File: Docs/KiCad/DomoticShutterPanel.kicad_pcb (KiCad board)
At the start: 2 copper layers, 110.6 x 50 mm, 7 parts

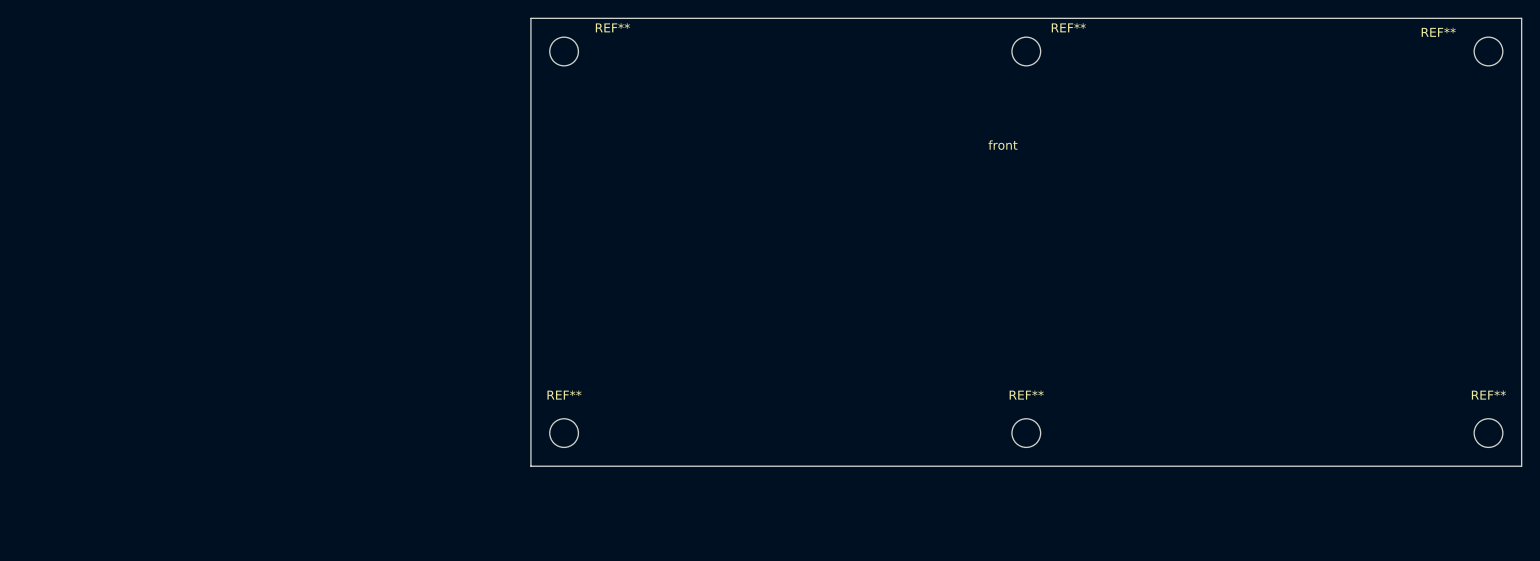
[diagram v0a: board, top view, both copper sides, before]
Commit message: Added buzzer and 3d model updated
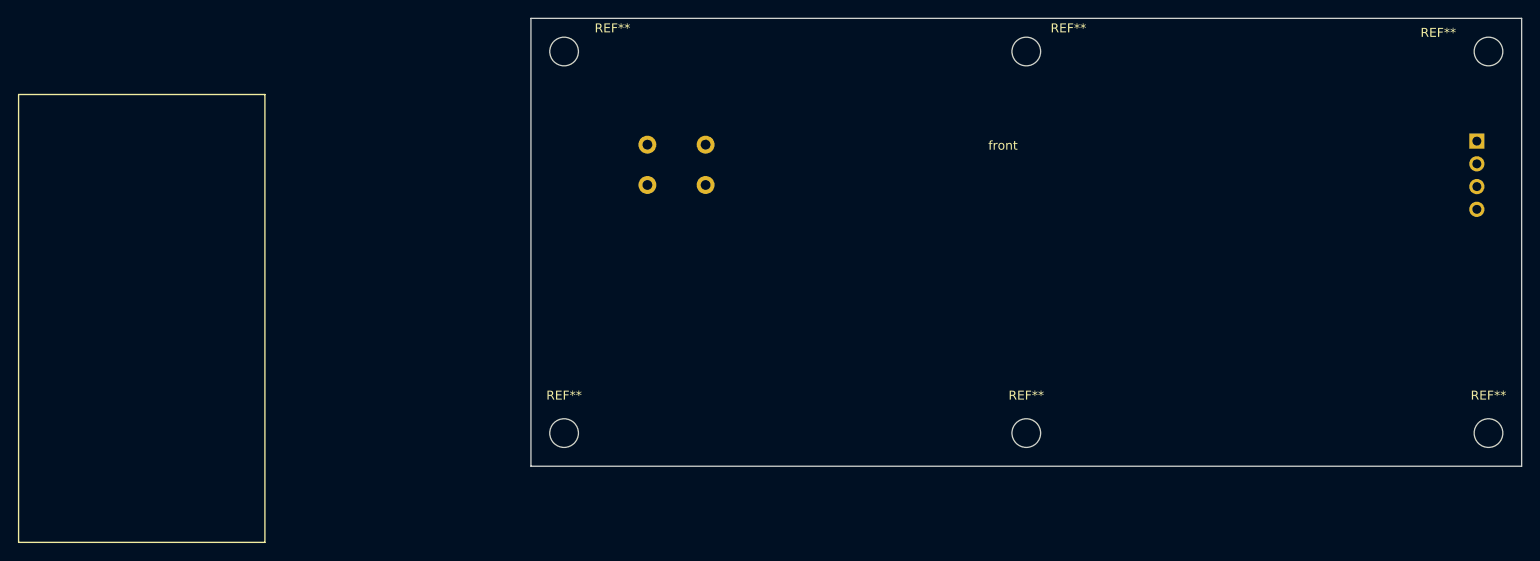
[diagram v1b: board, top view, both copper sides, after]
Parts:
- added REF**: SW_PUSH_6mm, Custom_libraries:SW_PUSH_6mm, B.Cu at (114.2, 89.1)
- added REF**: PinSocket_1x04_P2.54mm_Vertical, Connector_PinSocket_2.54mm:PinSocket_1x04_P2.54mm_Vertical, B.Cu at (200.3, 88.7)
